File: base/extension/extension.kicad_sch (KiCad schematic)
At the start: 22 parts, among them J1 USB_C_Receptacle_USB2.0_16P, J2 Conn_02x20_Odd_Even, J3 2-1734248-0, J4 Conn_01x02, J5 2-1734248-0, U1 LM7805_TO263, U2 MCP1700T-3302E/TT, U3 CH224K

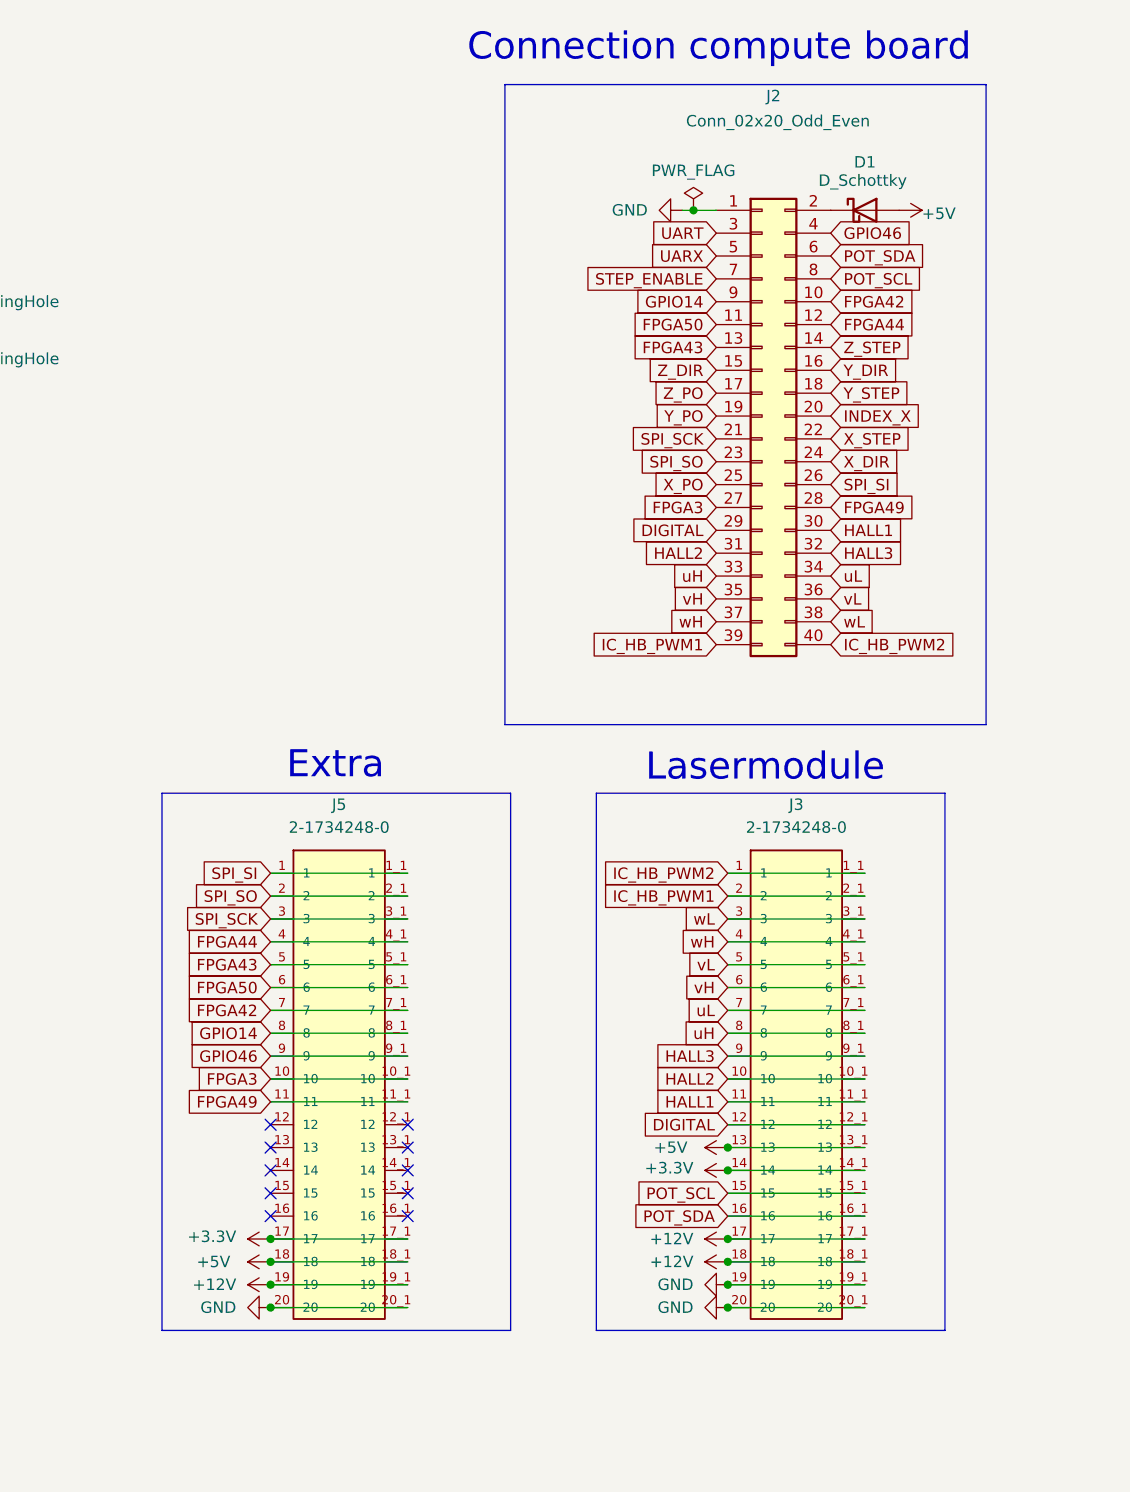
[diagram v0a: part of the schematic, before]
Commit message: fixes some mistake in the bom found in first assembly
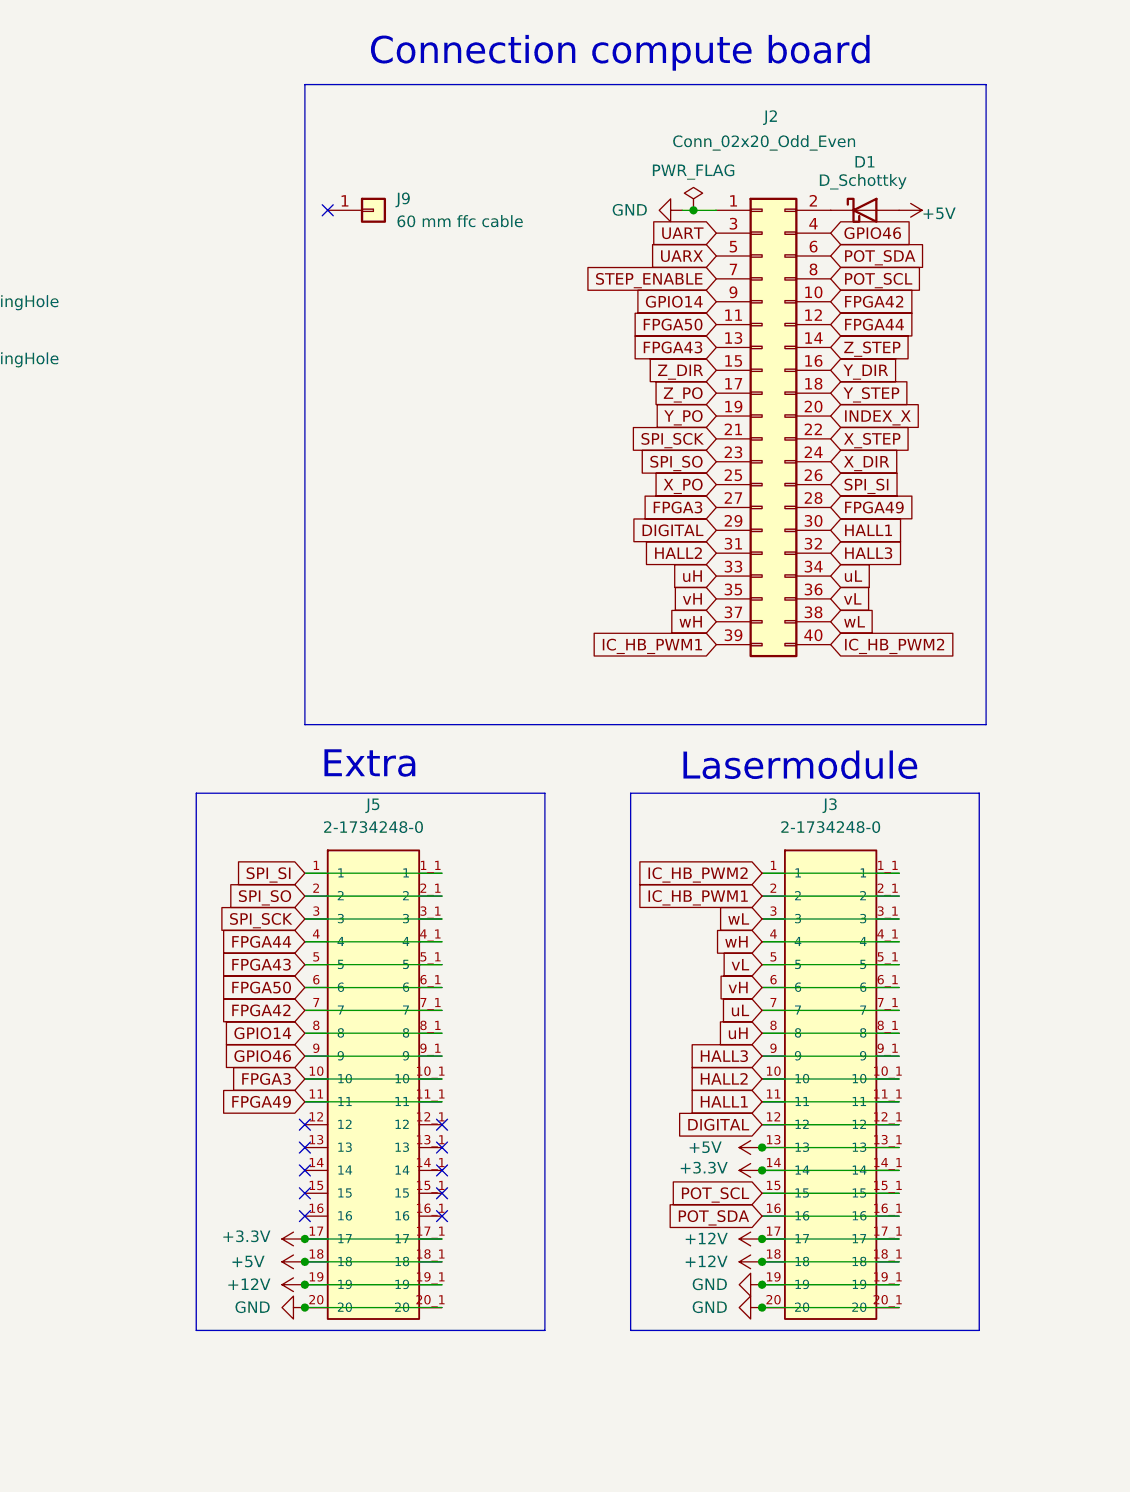
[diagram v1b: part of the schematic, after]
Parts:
- added J9: 60 mm ffc cable, symbol Connector_Generic:Conn_01x01
- C1: farnell# (none) -> 2094043
- G1: now left out of the parts list
- H1, H2: farnell# (none) -> 2987836; now in the parts list
- J2: farnell# 3817923 -> 3225919; manf# 61032021821 -> M20-7812045; mouser# 710-61032021821 -> 855-M20-7812045
- J4: manf# VN02A1500000G or 282834-2 -> VN02A1500000G
- R16: farnell# (none) -> 1469847
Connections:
- no-connect marks 13 -> 14
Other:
- moved on the sheet: J3, J5

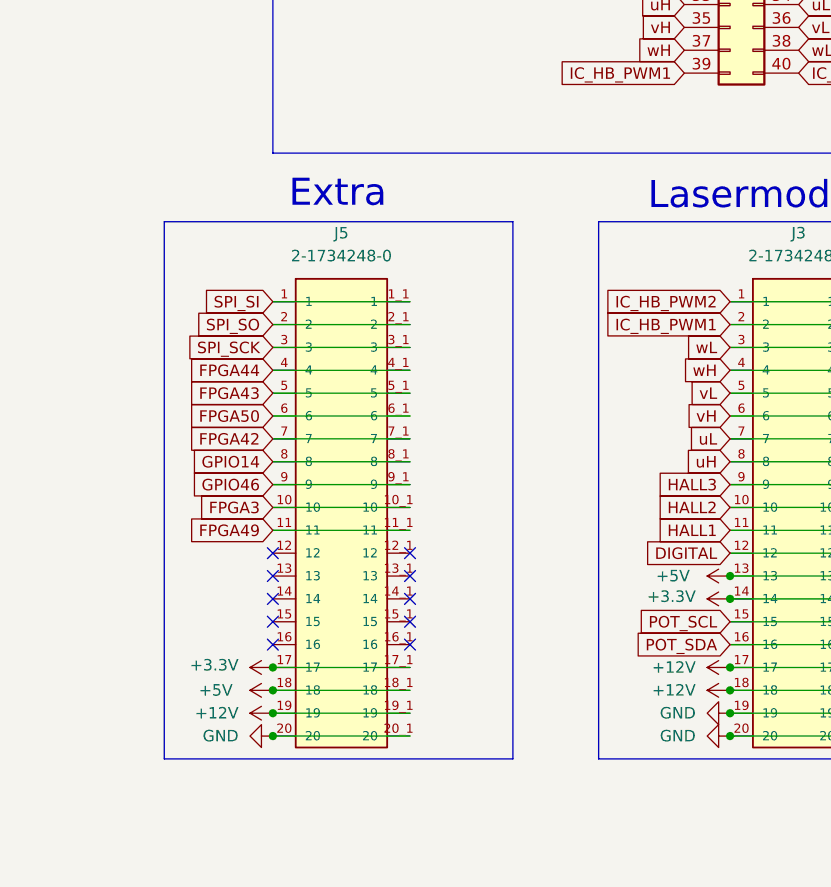
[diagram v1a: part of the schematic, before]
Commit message: fixed  issues uncovered with extension module
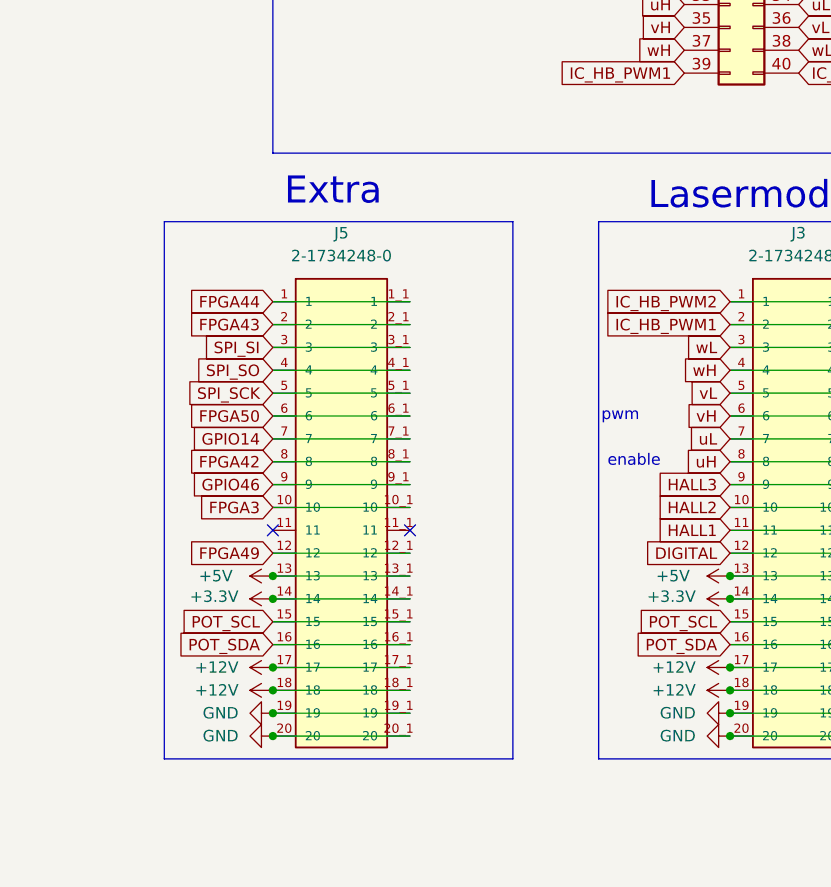
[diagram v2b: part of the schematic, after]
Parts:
- D1, D2, D3: footprint Diode_SMD:D_SOD-323_HandSoldering -> Diode_SMD:D_SMA; farnell# 2393466 -> 2335183; manf# SD103AWS-E3-08 -> B340A-E3/61T; mouser# 78-SD103AWS-HE3-18 -> 625-BD340A-E3/61T
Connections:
- net +12V: now also J5.17, J5.17_1 (17), J5.18, J5.18_1 (18); no longer J5.19, J5.19_1 (19)
- net +3.3V: now also J5.14, J5.14_1 (14); no longer J5.17, J5.17_1 (17)
- net +5V: now also J5.13, J5.13_1 (13); no longer J5.18, J5.18_1 (18)
- net FPGA42: now also J5.8, J5.8_1 (8); no longer J5.7, J5.7_1 (7)
- net FPGA43: now also J5.2, J5.2_1 (2); no longer J5.5, J5.5_1 (5)
- net FPGA44: now also J5.1, J5.1_1 (1); no longer J5.4, J5.4_1 (4)
- net FPGA49: now also J5.12, J5.12_1 (12); no longer J5.11, J5.11_1 (11)
- net GND: now also J5.19, J5.19_1 (19)
- net GPIO14: now also J5.7, J5.7_1 (7); no longer J5.8, J5.8_1 (8)
- net POT_SCL: now also J5.15, J5.15_1 (15)
- net POT_SDA: now also J5.16, J5.16_1 (16)
- net SPI_SCK: now also J5.5, J5.5_1 (5); no longer J5.3, J5.3_1 (3)
- net SPI_SI: now also J5.3, J5.3_1 (3); no longer J5.1, J5.1_1 (1)
- net SPI_SO: now also J5.4, J5.4_1 (4); no longer J5.2, J5.2_1 (2)
- no-connect marks 14 -> 6
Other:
- note added: "enable"
- note added: "pwm"

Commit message: fixed headers, shifted text base board
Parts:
- J2: farnell# 3225919 -> 2847933; manf# M20-7812045 -> 2214SM-40G-75-PCR; mouser# 855-M20-7812045 -> (none)
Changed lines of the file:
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@@
 			)
 		)
-		(property "mouser#" "855-M20-7812045"
+		(property "mouser#" ""
 			(at 251.46 57.15 0)
 			(effects
@@
 			)
 		)
-		(property "manf#" "M20-7812045"
+		(property "manf#" "2214SM-40G-75-PCR"
 			(at 251.46 57.15 0)
 			(effects
@@
 			)
 		)
-		(property "farnell#" "3225919"
+		(property "farnell#" "2847933"
 			(at 251.46 57.15 0)
 			(effects

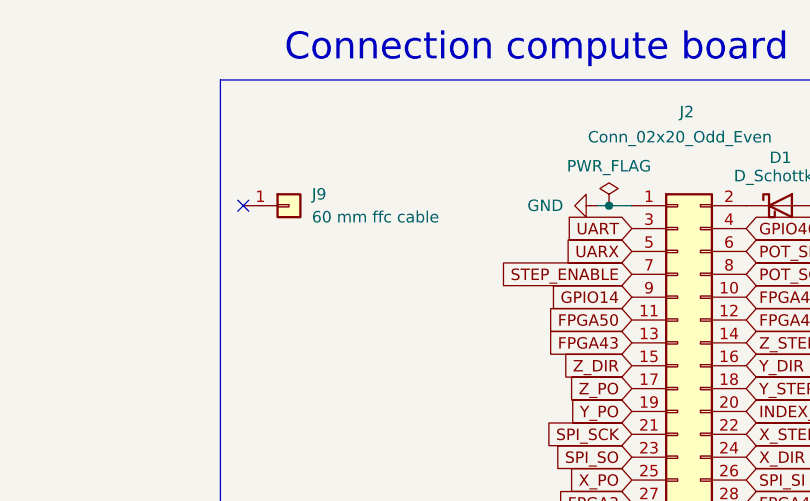
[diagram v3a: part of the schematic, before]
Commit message: added kicost notes
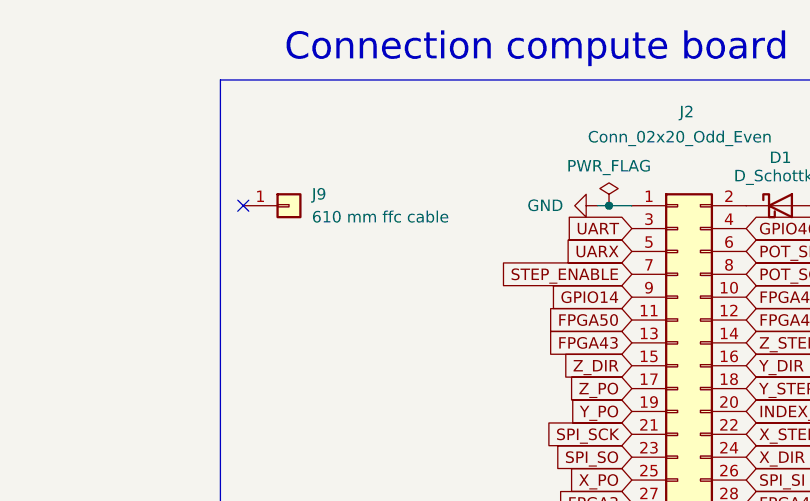
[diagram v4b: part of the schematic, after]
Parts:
- J9: value 60 mm ffc cable -> 610 mm ffc cable; farnell# 3514896 -> 3514895; manf# FJ-20-R-24.00-4 -> FJ-20-D-24.00-4
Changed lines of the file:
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@@
 			)
 		)
-		(property "Value" "60 mm ffc cable"
+		(property "Value" "610 mm ffc cable"
 			(at 210.82 35.5599 0)
 			(effects
@@
 			)
 		)
-		(property "farnell#" "3514896"
+		(property "farnell#" "3514895"
 			(at 208.28 34.29 0)
 			(effects
@@
 			)
 		)
-		(property "manf#" "FJ-20-R-24.00-4"
+		(property "manf#" "FJ-20-D-24.00-4"
 			(at 208.28 34.29 0)
 			(effects

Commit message: fixed pullups i2c
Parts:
- J4: Farnell 2112482 -> 3817460
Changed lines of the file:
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@@
 			)
 		)
-		(property "Farnell" "2112482"
+		(property "Farnell" "3817460"
 			(at 110.49 34.29 0)
 			(effects

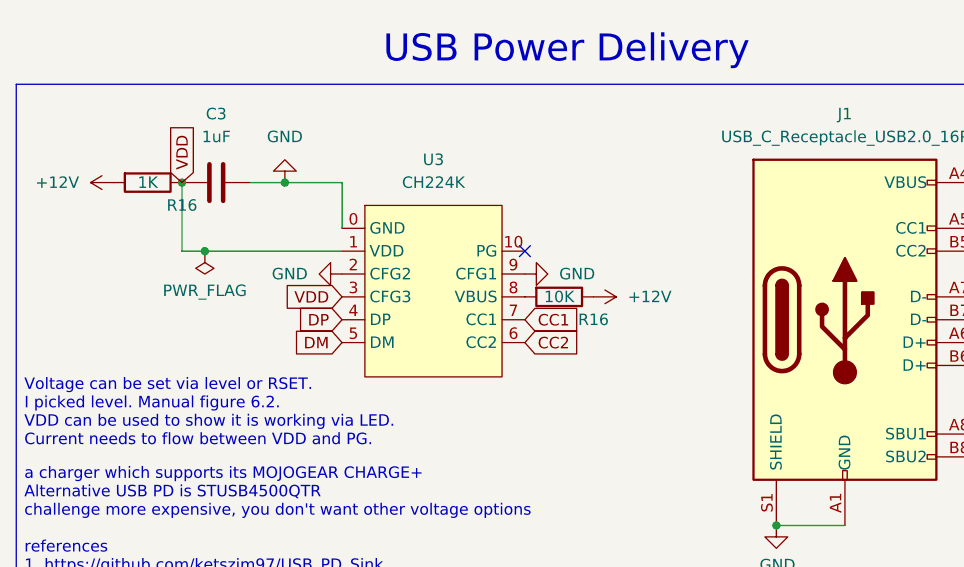
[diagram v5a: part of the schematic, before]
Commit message: compute board 4 layer, with camera connector and small bug fixes
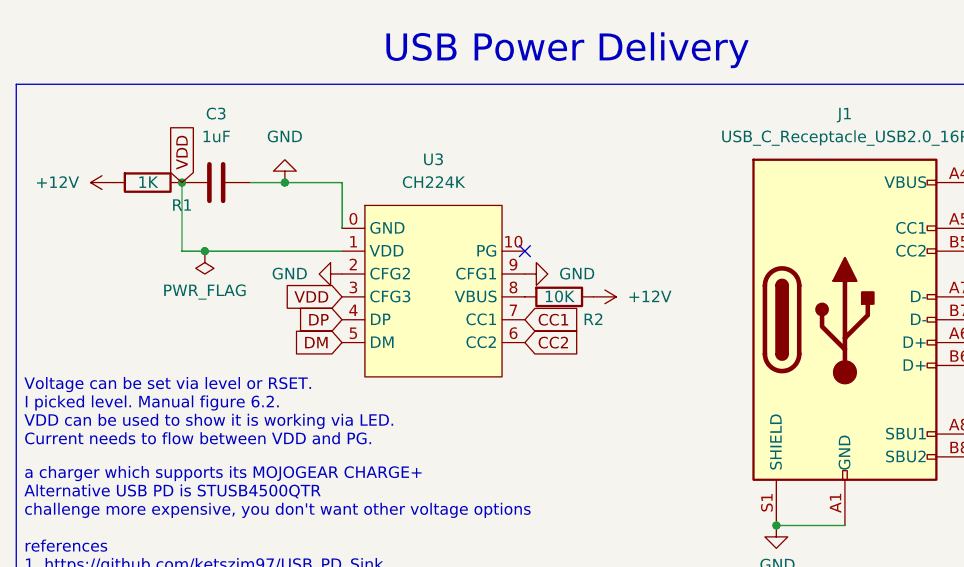
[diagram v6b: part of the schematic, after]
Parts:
- renumbered R16 to R1, R16 to R2

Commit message: schema  extension finished, pre  merge
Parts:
- removed C3: 1uF, Capacitor_SMD:C_0805_2012Metric_Pad1.18x1.45mm_HandSolder, symbol Device:C
- removed D1, D2: D_Schottky, Diode_SMD:D_SMA, symbol Device:D_Schottky
- removed J1: USB_C_Receptacle_USB2.0_16P, footprints:USB_C_Receptacle_GCT_USB4105-xx-A_16P_TopMnt_Horizontal, symbol Connector:USB_C_Receptacle_USB2.0_16P
- removed R1: 1K, Resistor_SMD:R_0805_2012Metric, symbol Device:R
- removed R2: 10K, Resistor_SMD:R_0805_2012Metric, symbol Device:R
- removed U3: CH224K, footprints:ESSOP-10_CH224K, symbol wch_mcu_peripheral:CH224K
- added C26: 470uF, Capacitor_SMD:CP_Elec_10x10.5, symbol Device:C_Polarized
- added Q1: Q_Dual_PMOS_S1G1S2G2D2D2D1D1, Package_SO:SOIC-8_3.9x4.9mm_P1.27mm, symbol Transistor_FET:Q_Dual_PMOS_S1G1S2G2D2D2D1D1
- C1, C5: value 1uF -> 10uF; Farnell 2094043 -> (none); farnell# 2094043 -> CL21A106KAYNNNE; manf# 08055C105KAT2A -> 187-CL21A106KAYNNNE; mouser# 581-08055C105KAT2A -> 3010126
- C2: value 1uF -> 10uF; farnell# 2094043 -> CL21A106KAYNNNE; manf# 08055C105KAT2A -> 187-CL21A106KAYNNNE; mouser# 581-08055C105KAT2A -> 3010126
- C4: value 0.1uF -> 10uF; Farnell 1414663 -> (none); farnell# 1414663 -> CL21A106KAYNNNE; manf# C0805C104J5RACTU -> 187-CL21A106KAYNNNE; mouser# 80-C0805C104J5R -> 3010126
- D3: value D_Schottky -> D_TVS; footprint Diode_SMD:D_SMA -> Diode_SMD:D_SMB; symbol Device:D_Schottky -> Device:D_TVS; farnell# 2335183 -> 2765106; manf# B340A-E3/61T -> SMBJ13CA; mouser# 625-BD340A-E3/61T -> 652-SMBJ13CA
- F1: footprint Fuse:Fuse_0603_1608Metric_Pad1.05x0.95mm_HandSolder -> Fuse:Fuse_2920_7451Metric; farnell# 2799441 -> 2336373; manf# SF-1206FP500-2 -> MF-LSMF300/24X-2; mouser# 652-SF-1206FP500-2 -> 652-MF-LSMF300/24X-2
- H1, H2: footprint MountingHole:MountingHole_2.2mm_M2 -> MountingHole:MountingHole_2.2mm_M2_Pad_Via; symbol Mechanical:MountingHole -> Mechanical:MountingHole_Pad; now left out of the parts list
- J2: mouser# (none) -> 649-221121-00040T4LF
- J3, J5: farnell# (none) -> 3404513
- J4: footprint footprints:VN02A1500000G -> Connector_BarrelJack:BarrelJack_CUI_PJ-036AH-SMT_Horizontal; symbol Connector_Generic:Conn_01x02 -> Connector:Jack-DC; Farnell 3817460 -> (none); farnell# (none) -> 4814431; manf# VN02A1500000G -> PJ-036AH-SMT-TR; mouser# 649-VN02A15000J0G -> 490-PJ-036AH-SMT-TR
- J9: mouser# (none) -> 538-15167-0361
- U1: farnell# (none) -> 2102566
- U2: farnell# (none) -> 1296592
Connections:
- net +12V: now also D3.1 (A1), C26.1, Q1.5 (D), Q1.6 (D), Q1.7 (D), Q1.8 (D); no longer F1.2
- net +5V: now also J2.2 (Pin_2)
- net GND: now also D3.2 (A2), H1.1, H2.1, J4.2, C26.2, Q1.2 (G), Q1.4 (G); no longer J4.1 (Pin_1)
- net GPIO46: now also J2.9 (Pin_9); no longer J2.4 (Pin_4)
- net GPIO14 renamed GPIO45
- net GPIO45: now also J2.4 (Pin_4); no longer J2.9 (Pin_9)
- net VBUS: no longer names the net of F1.1
- net VBUS: now also Q1.1 (S), Q1.3 (S); no longer D3.1 (K)
- new net: F1.2, J4.1
- no-connect marks 6 -> 3
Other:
- note removed: "USB Power Delivery"
- note removed: "Voltage can be set via level or RSET. I picked level. Manual figure 6.2. VDD can be used to show it is working via LED. Current needs to flow between VDD and PG."
- note removed: "a charger which supports its MOJOGEAR CHARGE+ Alternative USB PD is STUSB4500QTR challenge more expensive, you don't want other voltage options references 1. https://github.com/ketszim97/USB_PD_Sink 2. https://github.com/sparkfun/Power_Delivery_Board-USB-C"
- moved on the sheet: C1, C2, C4, C5, D3, F1, U1, U2
